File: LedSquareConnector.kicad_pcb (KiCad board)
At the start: 2 copper layers, 40.6 x 55.9 mm, 10 parts, among them J101 Conn_02x05_Odd_Even, J102 Conn_02x05_Odd_Even, J103 Conn_02x05_Odd_Even, J104 Conn_02x05_Odd_Even

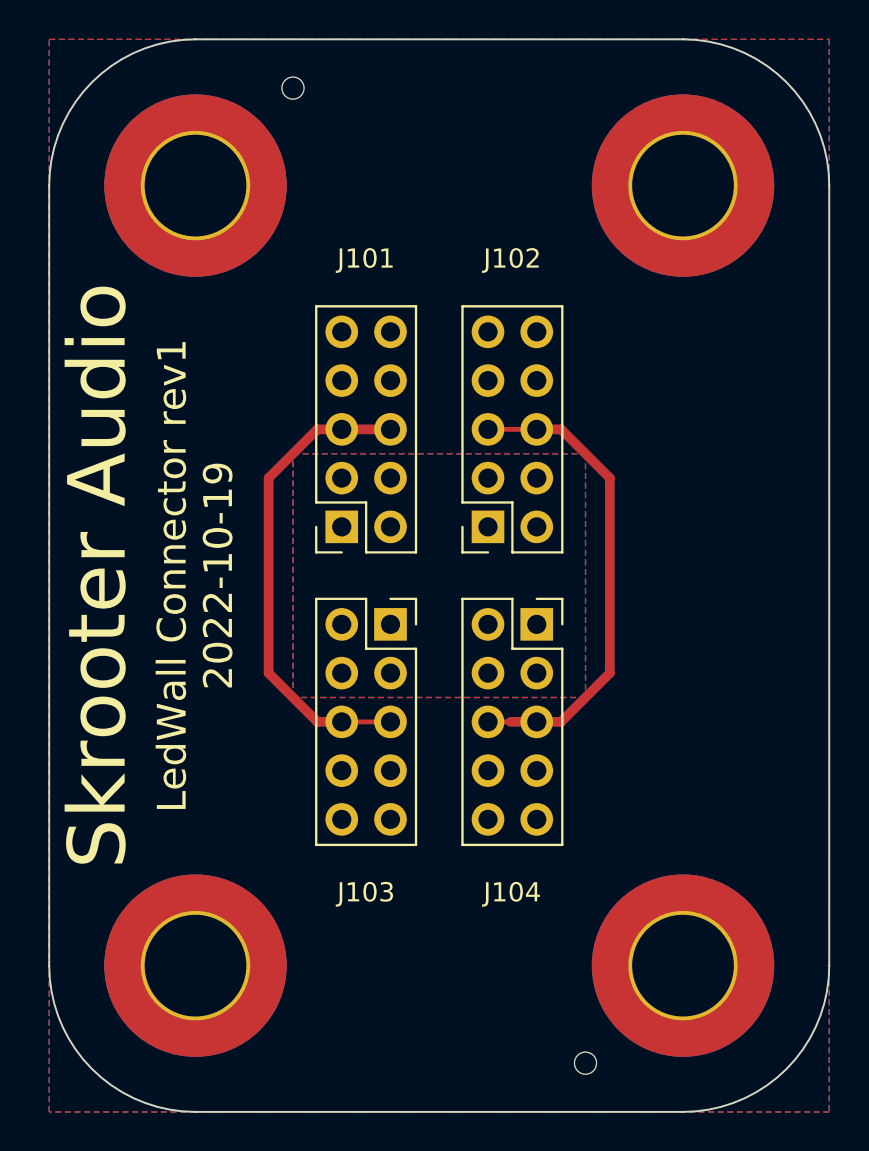
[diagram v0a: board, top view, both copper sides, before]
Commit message: Change connector and prep for manufactoring
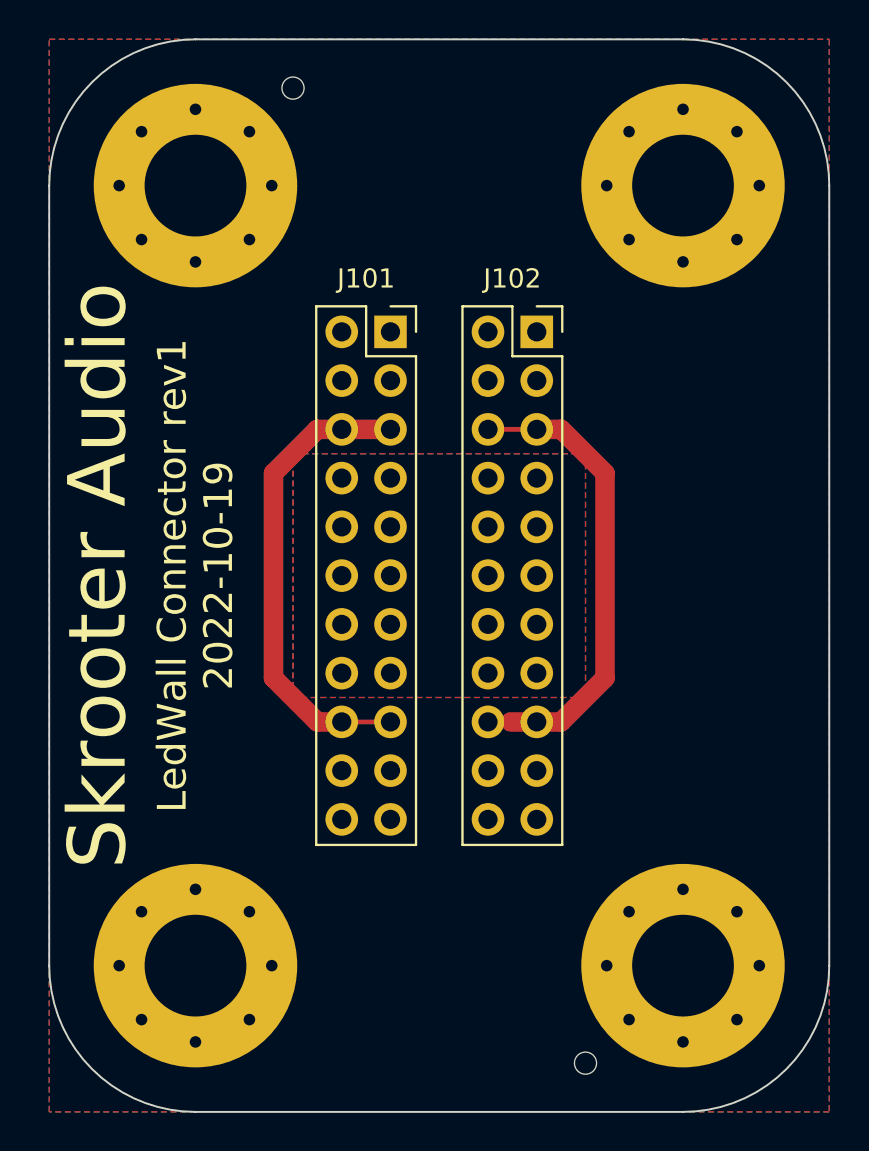
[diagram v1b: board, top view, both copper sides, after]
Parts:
- removed J103, J104: Conn_02x05_Odd_Even, Connector_PinSocket_2.54mm:PinSocket_2x05_P2.54mm_Vertical
- H101, H102, H103, H104: footprint MountingHole:MountingHole_5.3mm_M5_ISO7380_Pad_TopBottom -> MountingHole:MountingHole_5.3mm_M5_Pad_Via
- J101, J102: value Conn_02x05_Odd_Even -> Conn_02x11_Odd_Even; footprint Connector_PinSocket_2.54mm:PinSocket_2x05_P2.54mm_Vertical -> Connector_PinSocket_2.54mm:PinSocket_2x11_P2.54mm_Vertical
- moved J101 10.5 mm to (83.8, 55.9), turned to 0 degrees
- moved J102 10.5 mm to (91.4, 55.9), turned to 0 degrees
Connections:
- J101 pad 1: VDC -> GND
- J101 pad 10: GND -> VDC
- J101 pad 2: VDC -> GND
- J101 pad 3: VDC -> GND
- J101 pad 4: VDC -> GND
- J101 pad 7: GND -> VDC
- J101 pad 8: GND -> VDC
- J101 pad 9: GND -> VDC
- J102 pad 1: VDC -> GND
- J102 pad 10: GND -> VDC
- J102 pad 2: VDC -> GND
- J102 pad 3: VDC -> GND
- J102 pad 4: VDC -> GND
- J102 pad 7: GND -> VDC
- J102 pad 8: GND -> VDC
- J102 pad 9: GND -> VDC

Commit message: Revert last commit and move upper header 50 mil
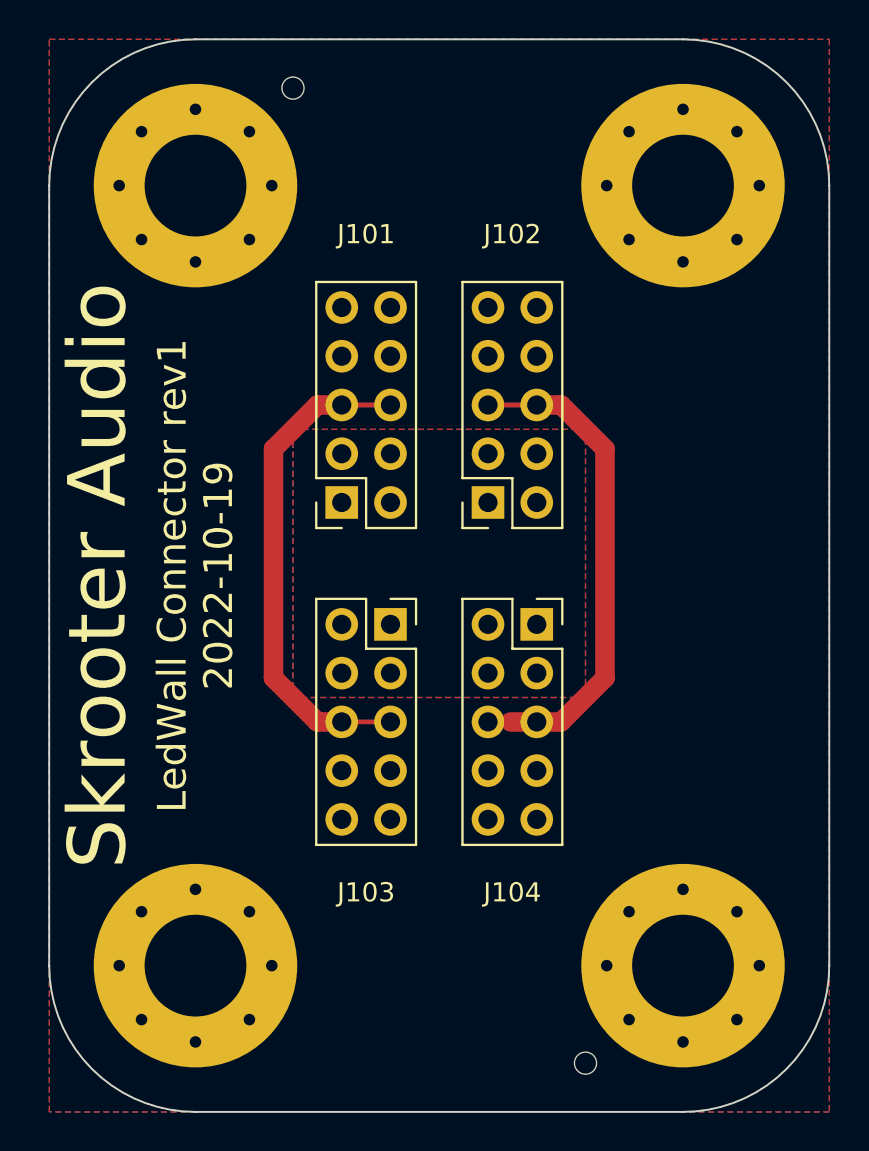
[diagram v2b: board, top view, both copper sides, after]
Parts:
- added J103: Conn_02x05_Odd_Even, Connector_PinSocket_2.54mm:PinSocket_2x05_P2.54mm_Vertical, F.Cu at (83.8, 71.1)
- added J104: Conn_02x05_Odd_Even, Connector_PinSocket_2.54mm:PinSocket_2x05_P2.54mm_Vertical, F.Cu at (91.4, 71.1)
- J101, J102: value Conn_02x11_Odd_Even -> Conn_02x05_Odd_Even; footprint Connector_PinSocket_2.54mm:PinSocket_2x11_P2.54mm_Vertical -> Connector_PinSocket_2.54mm:PinSocket_2x05_P2.54mm_Vertical
- moved J101 9.25 mm to (81.3, 64.8), turned to 180 degrees
- moved J102 9.25 mm to (88.9, 64.8), turned to 180 degrees
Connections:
- J101 pad 1: GND -> VDC
- J101 pad 10: VDC -> GND
- J101 pad 2: GND -> VDC
- J101 pad 3: GND -> VDC
- J101 pad 4: GND -> VDC
- J101 pad 7: VDC -> GND
- J101 pad 8: VDC -> GND
- J101 pad 9: VDC -> GND
- J102 pad 1: GND -> VDC
- J102 pad 10: VDC -> GND
- J102 pad 2: GND -> VDC
- J102 pad 3: GND -> VDC
- J102 pad 4: GND -> VDC
- J102 pad 7: VDC -> GND
- J102 pad 8: VDC -> GND
- J102 pad 9: VDC -> GND
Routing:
- net /Data: track 24.8 -> 26.0 mm
- net /EN: track 26.1 -> 27.4 mm

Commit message: Add LCSC partnumbers to headers
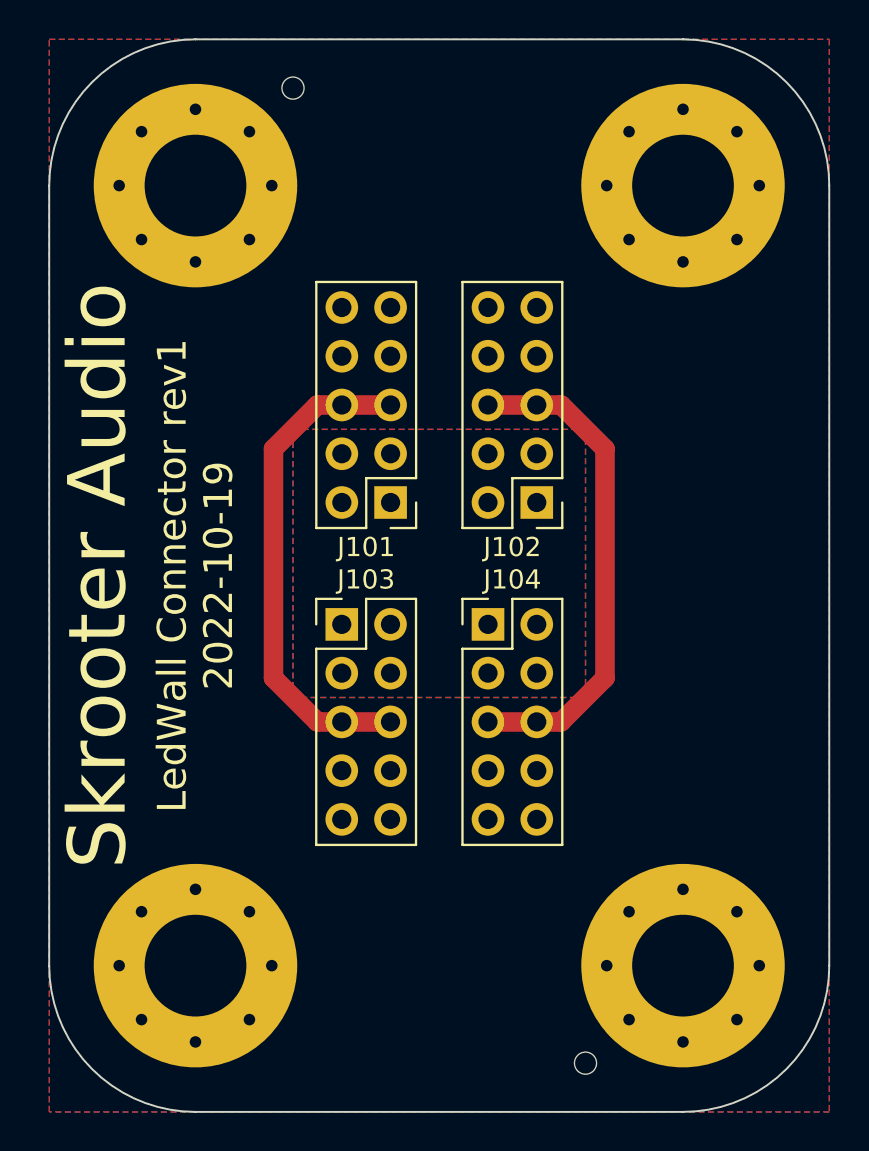
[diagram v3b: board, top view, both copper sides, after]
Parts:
- J101, J102, J103, J104: footprint Connector_PinSocket_2.54mm:PinSocket_2x05_P2.54mm_Vertical -> Connector_PinHeader_2.54mm:PinHeader_2x05_P2.54mm_Vertical
- moved J101 2.55 mm to (83.8, 64.8)
- moved J102 2.54 mm to (91.4, 64.8)
- moved J103 2.54 mm to (81.3, 71.1)
- moved J104 2.54 mm to (88.9, 71.1)
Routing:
- net /EN: track 27.4 -> 26.0 mm
